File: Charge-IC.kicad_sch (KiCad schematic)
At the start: 34 parts, among them Q1 RSJ250P10, Q2 RSJ250P10, SW1 SW_DPDT_x2, SW2 SW_SPDT, U2 LTC4000-QFN

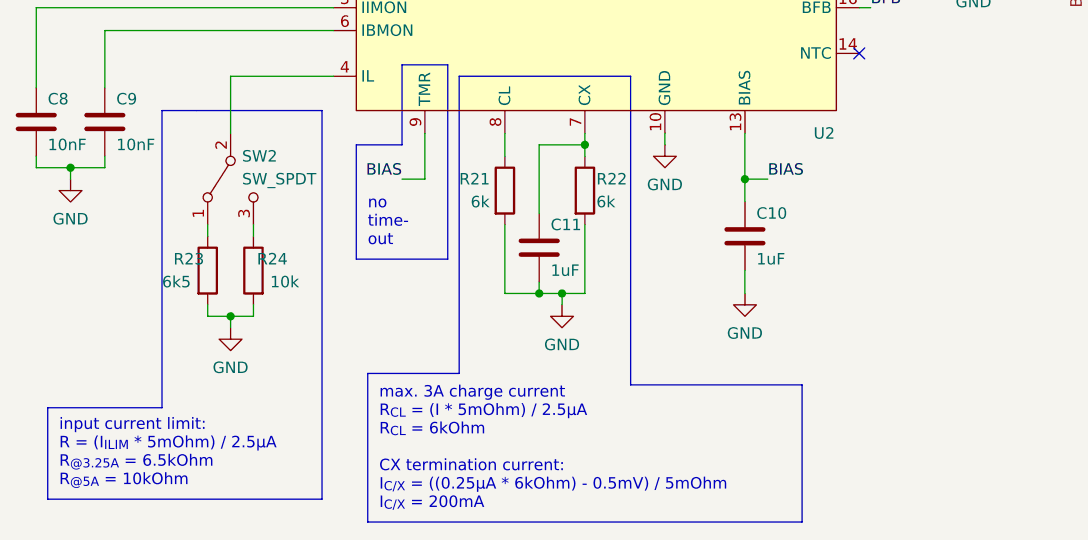
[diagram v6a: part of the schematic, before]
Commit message: Update BOM due component order
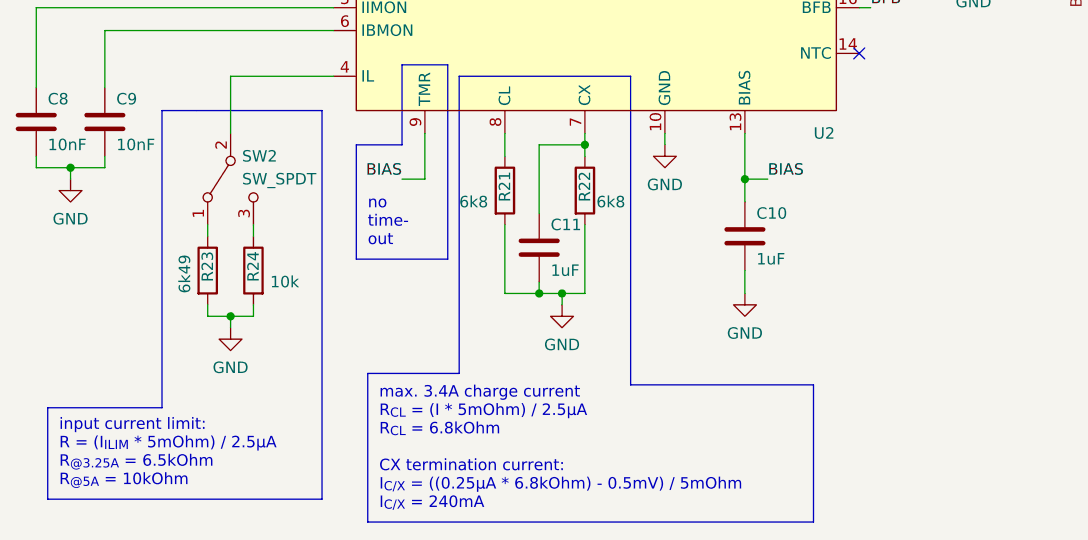
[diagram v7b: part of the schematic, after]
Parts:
- R21, R22: value 6k -> 6k8
- R23: value 6k5 -> 6k49
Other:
- note added: "max. 3.4A charge current R_{CL} = (I * 5mOhm) / 2.5µA R_{CL} = 6.8kOhm CX termination current: I_{C/X} = ((0.25µA * 6.8kOhm) - 0.5mV) / 5mOhm I_{C/X} = 240mA"
- note removed: "max. 3A charge current R_{CL} = (I * 5mOhm) / 2.5µA R_{CL} = 6kOhm CX termination current: I_{C/X} = ((0.25µA * 6kOhm) - 0.5mV) / 5mOhm I_{C/X} = 200mA"
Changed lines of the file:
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@@
     (stroke (width 0) (type default) (color 0 0 0 0))
   )
-  (polyline (pts (xy 105.41 161.29) (xy 105.41 176.53))
+  (polyline (pts (xy 106.68 161.29) (xy 106.68 176.53))
     (stroke (width 0) (type default) (color 0 0 0 0))
   )
@@
     (stroke (width 0) (type default) (color 0 0 0 0))
   )
-  (polyline (pts (xy 105.41 176.53) (xy 57.15 176.53))
+  (polyline (pts (xy 106.68 176.53) (xy 57.15 176.53))
     (stroke (width 0) (type default) (color 0 0 0 0))
   )
@@
     (stroke (width 0) (type default) (color 0 0 0 0))
   )
-  (polyline (pts (xy 86.36 161.29) (xy 105.41 161.29))
+  (polyline (pts (xy 86.36 161.29) (xy 106.68 161.29))
     (stroke (width 0) (type default) (color 0 0 0 0))
   )
@@
     (effects (font (size 1.27 1.27)) (justify left bottom))
   )
-  (text "max. 3A charge current\nR_{CL} = (I * 5mOhm) / 2.5µA \nR_{CL} = 6kOhm\n\nCX termination current:\nI_{C/X} = ((0.25µA * 6kOhm) - 0.5mV) / 5mOhm\nI_{C/X} = 200mA"
+  (text "max. 3.4A charge current\nR_{CL} = (I * 5mOhm) / 2.5µA \nR_{CL} = 6.8kOhm\n\nCX termination current:\nI_{C/X} = ((0.25µA * 6.8kOhm) - 0.5mV) / 5mOhm\nI_{C/X} = 240mA"
     (at 58.42 175.26 0)
     (effects (font (size 1.27 1.27)) (justify left bottom))
@@
   (symbol (lib_id "Device:R") (at 81.28 139.7 0) (unit 1)
     (in_bom yes) (on_board yes)
-    (property "Reference" "R22" (id 0) (at 82.55 138.43 0)
-      (effects (font (size 1.27 1.27)) (justify left))
-    )
-    (property "Value" "6k" (id 1) (at 82.55 140.97 0)
+    (property "Reference" "R22" (id 0) (at 81.28 140.97 90)
+      (effects (font (size 1.27 1.27)) (justify left))
+    )
+    (property "Value" "6k8" (id 1) (at 82.55 140.97 0)
       (effects (font (size 1.27 1.27)) (justify left))
     )
@@
   (symbol (lib_id "Device:R") (at 39.37 148.59 0) (unit 1)
     (in_bom yes) (on_board yes)
-    (property "Reference" "R23" (id 0) (at 35.56 147.32 0)
-      (effects (font (size 1.27 1.27)) (justify left))
-    )
-    (property "Value" "6k5" (id 1) (at 34.29 149.86 0)
+    (property "Reference" "R23" (id 0) (at 39.37 149.86 90)
+      (effects (font (size 1.27 1.27)) (justify left))
+    )
+    (property "Value" "6k49" (id 1) (at 36.83 151.13 90)
       (effects (font (size 1.27 1.27)) (justify left))
     )
@@
   (symbol (lib_id "Device:R") (at 72.39 139.7 0) (unit 1)
     (in_bom yes) (on_board yes)
-    (property "Reference" "R21" (id 0) (at 67.31 138.43 0)
-      (effects (font (size 1.27 1.27)) (justify left))
-    )
-    (property "Value" "6k" (id 1) (at 68.58 140.97 0)
+    (property "Reference" "R21" (id 0) (at 72.39 140.97 90)
+      (effects (font (size 1.27 1.27)) (justify left))
+    )
+    (property "Value" "6k8" (id 1) (at 67.31 140.97 0)
       (effects (font (size 1.27 1.27)) (justify left))
     )
@@
   (symbol (lib_id "Device:R") (at 44.45 148.59 0) (mirror y) (unit 1)
     (in_bom yes) (on_board yes)
-    (property "Reference" "R24" (id 0) (at 48.26 147.32 0)
-      (effects (font (size 1.27 1.27)) (justify left))
-    )
+    (property "Reference" "R24" (id 0) (at 44.45 149.86 90)
+      (effects (font (size 1.27 1.27)) (justify left))
+    )
